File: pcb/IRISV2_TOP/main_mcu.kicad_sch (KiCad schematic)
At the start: 38 parts, among them IC1 ATA6561-GAQW-N, J10 Conn_02x04_Odd_Even, J4 Screw_Terminal_01x03, U4 STM32H563VITx, Y1 25mHz 8pf, Y2 32.768kHz 12.5pF

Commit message: most routing done inc some reassignment, pretty much just connectors left now
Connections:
- net mpu_i2c2_sda is gone; now on net icm1_cs: U4.51 (PB12)
- net bmp_cs: now also U4.77 (PA15(JTDI)); no longer U4.84 (PD3)
- net bmp_int: now also U4.83 (PD2); no longer U4.85 (PD4)
- net can_stby: now also U4.84 (PD3); no longer U4.83 (PD2)
- net icm1_cs: no longer U4.46 (PE15)
- net icm1_int: now also U4.57 (PD10); no longer U4.45 (PE14)
- net icm2_cs: now also U4.29 (PA4); no longer U4.33 (PC4)
- net icm2_int: now also U4.33 (PC4); no longer U4.34 (PC5)
- net icm_fsync: now also U4.45 (PE14); no longer U4.60 (PD13)
- net mpu_i2c2_scl: no longer names the net of U4.47 (PB10)
- no-connect marks 2 -> 1

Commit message: all main routing done, need to break out remaining gpio onto banks of mpu and ppu
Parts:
- removed D5: STATUS, LED_SMD:LED_0805_2012Metric, symbol Device:LED
- removed J4: Screw_Terminal_01x03, symbol Connector:Screw_Terminal_01x03
- removed R19: 120, Resistor_SMD:R_0603_1608Metric, symbol Device:R
- added D1: STATUS, LED_SMD:LED_0805_2012Metric, symbol Device:LED
- added R24: 120, Resistor_SMD:R_0603_1608Metric, symbol Device:R
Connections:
- net GND: now also R24.1
- net at U4.38 (PE7): now also D1.2 (A)
- new net: D1.1 (K), R24.2

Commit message: removed usb, added connectors and stuff, 3d models mostly added, still need to route out gpio and servos (though connectors added)
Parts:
- removed J10: Conn_02x04_Odd_Even, Connector_PinHeader_2.54mm:PinHeader_2x04_P2.54mm_Vertical, symbol Connector_Generic:Conn_02x04_Odd_Even
- added J11, J12: Conn_01x04_MountingPin, Connector_JST:JST_PH_S4B-PH-SM4-TB_1x04-1MP_P2.00mm_Horizontal, symbol Connector_Generic_MountingPin:Conn_01x04_MountingPin
- added J5: Conn_02x15_Odd_Even, 10164227-0304A1RLF:AMPHENOL_10164227-0305A1RLF, symbol Connector_Generic:Conn_02x15_Odd_Even
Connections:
- net GND: now also J11.MP (MountPin), J12.MP (MountPin)
- net pwm1: now also J11.1 (Pin_1)
- net pwm2: now also J11.2 (Pin_2)
- net pwm3: now also J11.3 (Pin_3)
- net pwm4: now also J11.4 (Pin_4)
- net pwm5: now also J12.1 (Pin_1)
- net pwm6: now also J12.2 (Pin_2)
- net pwm7: now also J12.3 (Pin_3)
- net pwm8: now also J12.4 (Pin_4)
- net boot renamed mcu_boot
- net rst renamed mcu_rst
- net swclk renamed mcu_swclk
- net swdio renamed mcu_swdio
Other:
- note added: "33 free gpio"
- note added: "pwm (servo) connectors"
- note removed: "debug"

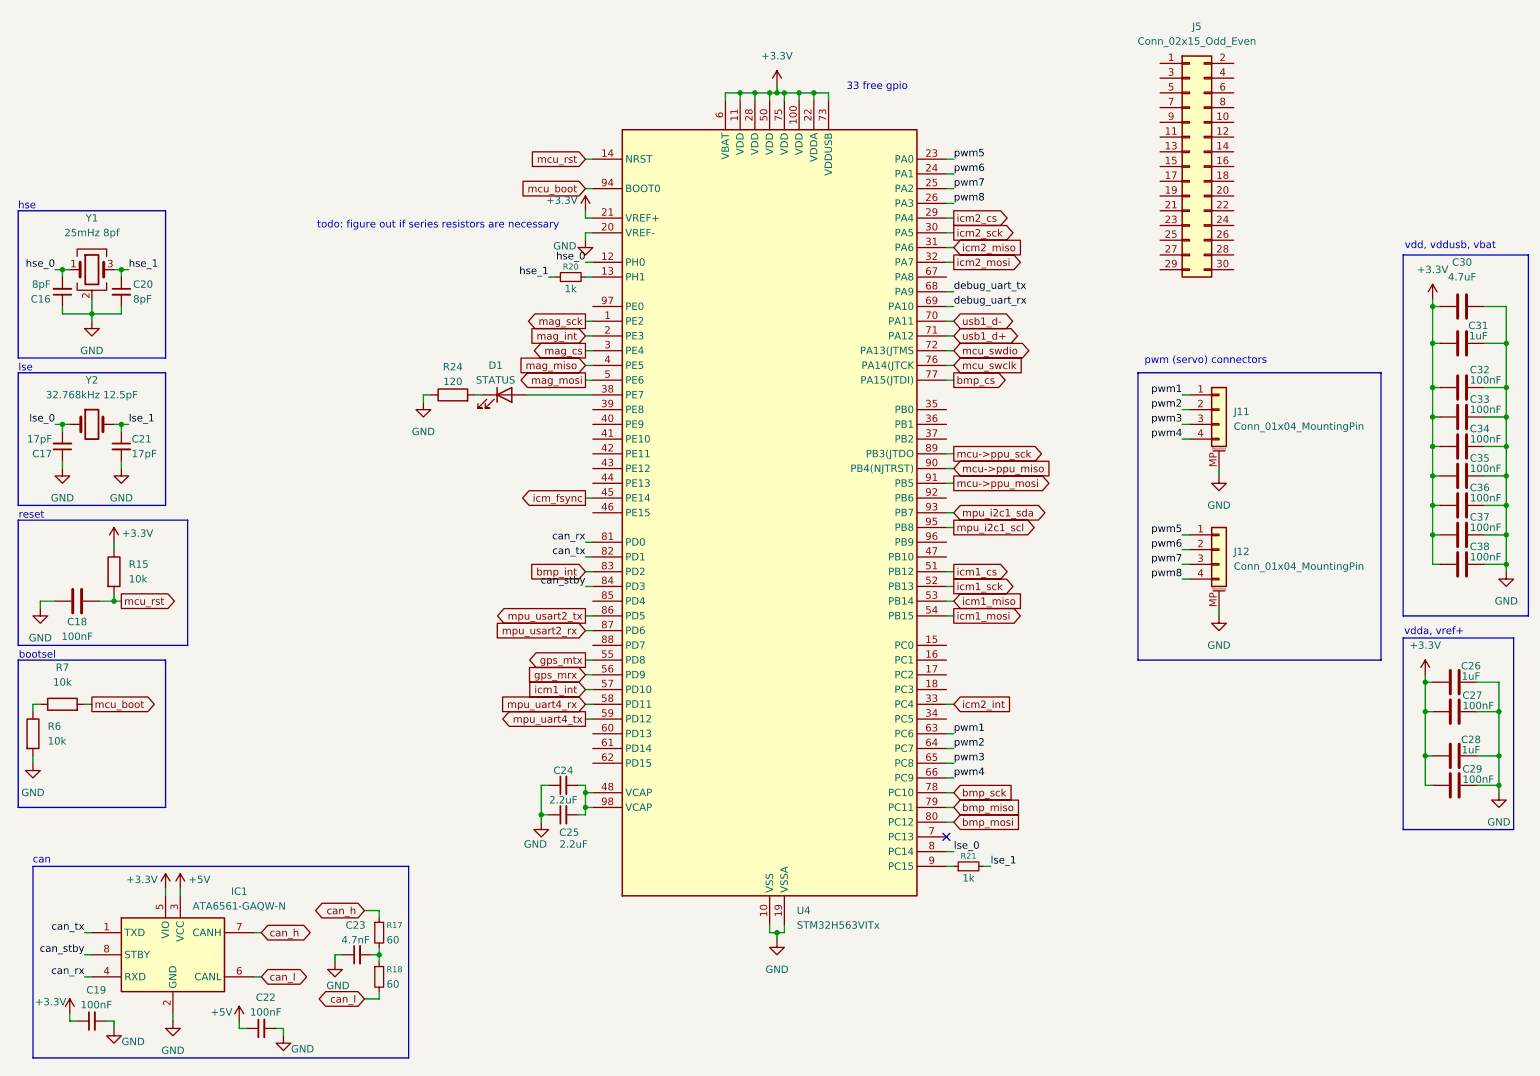
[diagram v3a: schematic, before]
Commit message: 3d models nearly done, just missing a few, gpio header routed - about to change lr2021 trace width
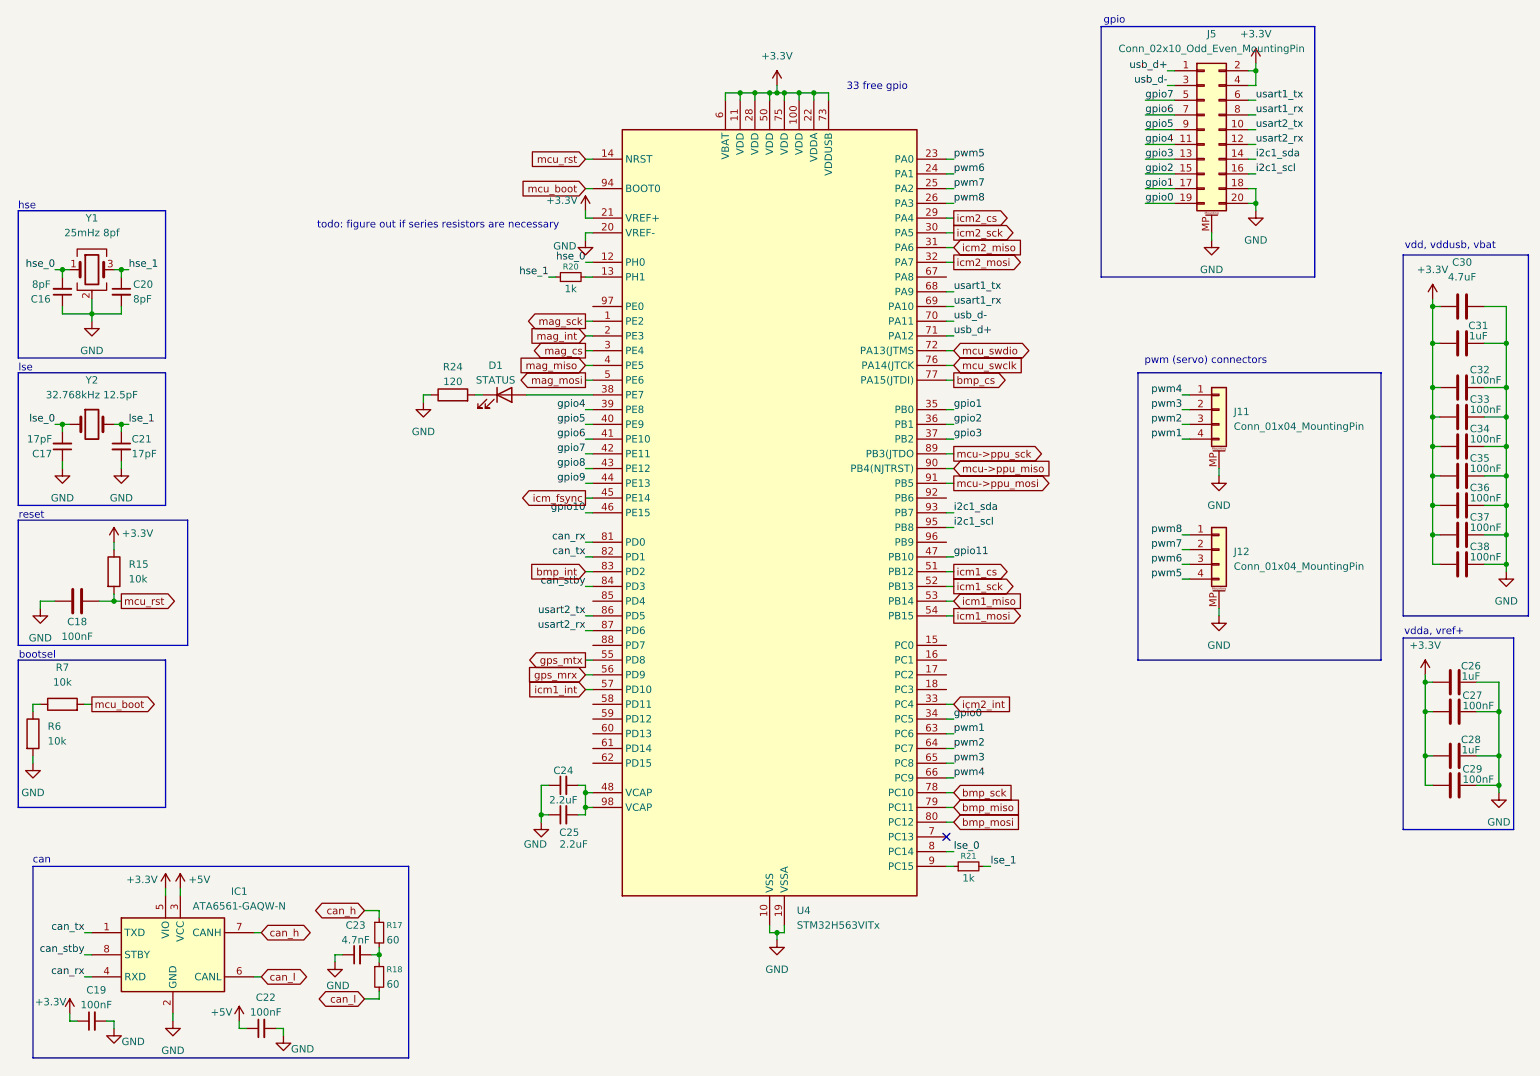
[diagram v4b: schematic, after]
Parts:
- removed J5: Conn_02x15_Odd_Even, 10164227-0304A1RLF:AMPHENOL_10164227-0305A1RLF, symbol Connector_Generic:Conn_02x15_Odd_Even
- added J5: Conn_02x10_Odd_Even_MountingPin, 10164228-0201A1RLF:AMPHENOL_10164228-0201A1RLF, symbol Connector_Generic_MountingPin:Conn_02x10_Odd_Even_MountingPin
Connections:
- net +3.3V: now also J5.2 (Pin_2), J5.4 (Pin_4)
- net GND: now also J5.18 (Pin_18), J5.20 (Pin_20), J5.MP (MountPin)
- net pwm1: now also J11.4 (Pin_4); no longer J11.1 (Pin_1)
- net pwm2: now also J11.3 (Pin_3); no longer J11.2 (Pin_2)
- net pwm3: now also J11.2 (Pin_2); no longer J11.3 (Pin_3)
- net pwm4: now also J11.1 (Pin_1); no longer J11.4 (Pin_4)
- net pwm5: now also J12.4 (Pin_4); no longer J12.1 (Pin_1)
- net pwm6: now also J12.3 (Pin_3); no longer J12.2 (Pin_2)
- net pwm7: now also J12.2 (Pin_2); no longer J12.3 (Pin_3)
- net pwm8: now also J12.1 (Pin_1); no longer J12.4 (Pin_4)
- net gpio0: now reaches U4.34 (PC5)
- net gpio0: now also J5.19 (Pin_19)
- net gpio1: now reaches U4.35 (PB0)
- net gpio1: now also J5.17 (Pin_17)
- net gpio2: now reaches U4.36 (PB1)
- net gpio2: now also J5.15 (Pin_15)
- net gpio3: now reaches U4.37 (PB2)
- net gpio3: now also J5.13 (Pin_13)
- net gpio4: now reaches U4.39 (PE8)
- net gpio4: now also J5.11 (Pin_11)
- net gpio5: now reaches U4.40 (PE9)
- net gpio5: now also J5.9 (Pin_9)
- net gpio6: now reaches U4.41 (PE10)
- net gpio6: now also J5.7 (Pin_7)
- net gpio7: now reaches U4.42 (PE11)
- net gpio7: now also J5.5 (Pin_5)
- net gpio8: now reaches U4.43 (PE12)
- net gpio9: now reaches U4.44 (PE13)
- net gpio10: now reaches U4.46 (PE15)
- net gpio11: now reaches U4.47 (PB10)
- net debug_uart_rx renamed usart1_rx
- net usart1_rx: now also J5.8 (Pin_8)
- net debug_uart_tx renamed usart1_tx
- net usart1_tx: now also J5.6 (Pin_6)
- net mpu_i2c1_scl renamed i2c1_scl
- net i2c1_scl: now also J5.16 (Pin_16)
- net mpu_i2c1_sda renamed i2c1_sda
- net i2c1_sda: now also J5.14 (Pin_14)
- net mpu_uart4_rx: no longer names the net of U4.58 (PD11)
- net mpu_uart4_tx: no longer names the net of U4.59 (PD12)
- net mpu_usart2_rx renamed usart2_rx
- net usart2_rx: now also J5.12 (Pin_12)
- net mpu_usart2_tx renamed usart2_tx
- net usart2_tx: now also J5.10 (Pin_10)
- net usb1_d+ renamed usb_d+
- net usb_d+: now also J5.1 (Pin_1)
- net usb1_d- renamed usb_d-
- net usb_d-: now also J5.3 (Pin_3)
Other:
- note added: "gpio"

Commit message: pcb hopefully mostly finalized
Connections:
- net cam_uart_rx: now reaches U4.58 (PD11)
- net cam_uart_tx: now reaches U4.59 (PD12)
- net gpio10: no longer names the net of U4.46 (PE15)
- net gpio8: no longer names the net of U4.43 (PE12)
- net gpio9: no longer names the net of U4.44 (PE13)
